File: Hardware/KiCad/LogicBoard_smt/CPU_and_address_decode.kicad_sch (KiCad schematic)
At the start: 20 parts, among them IC12 7408N, IC16 7404N, IC32 7432N, IC4 7404N, IC53 7404N, IC7 7408N, U1 W65C02SP, U2 VIA

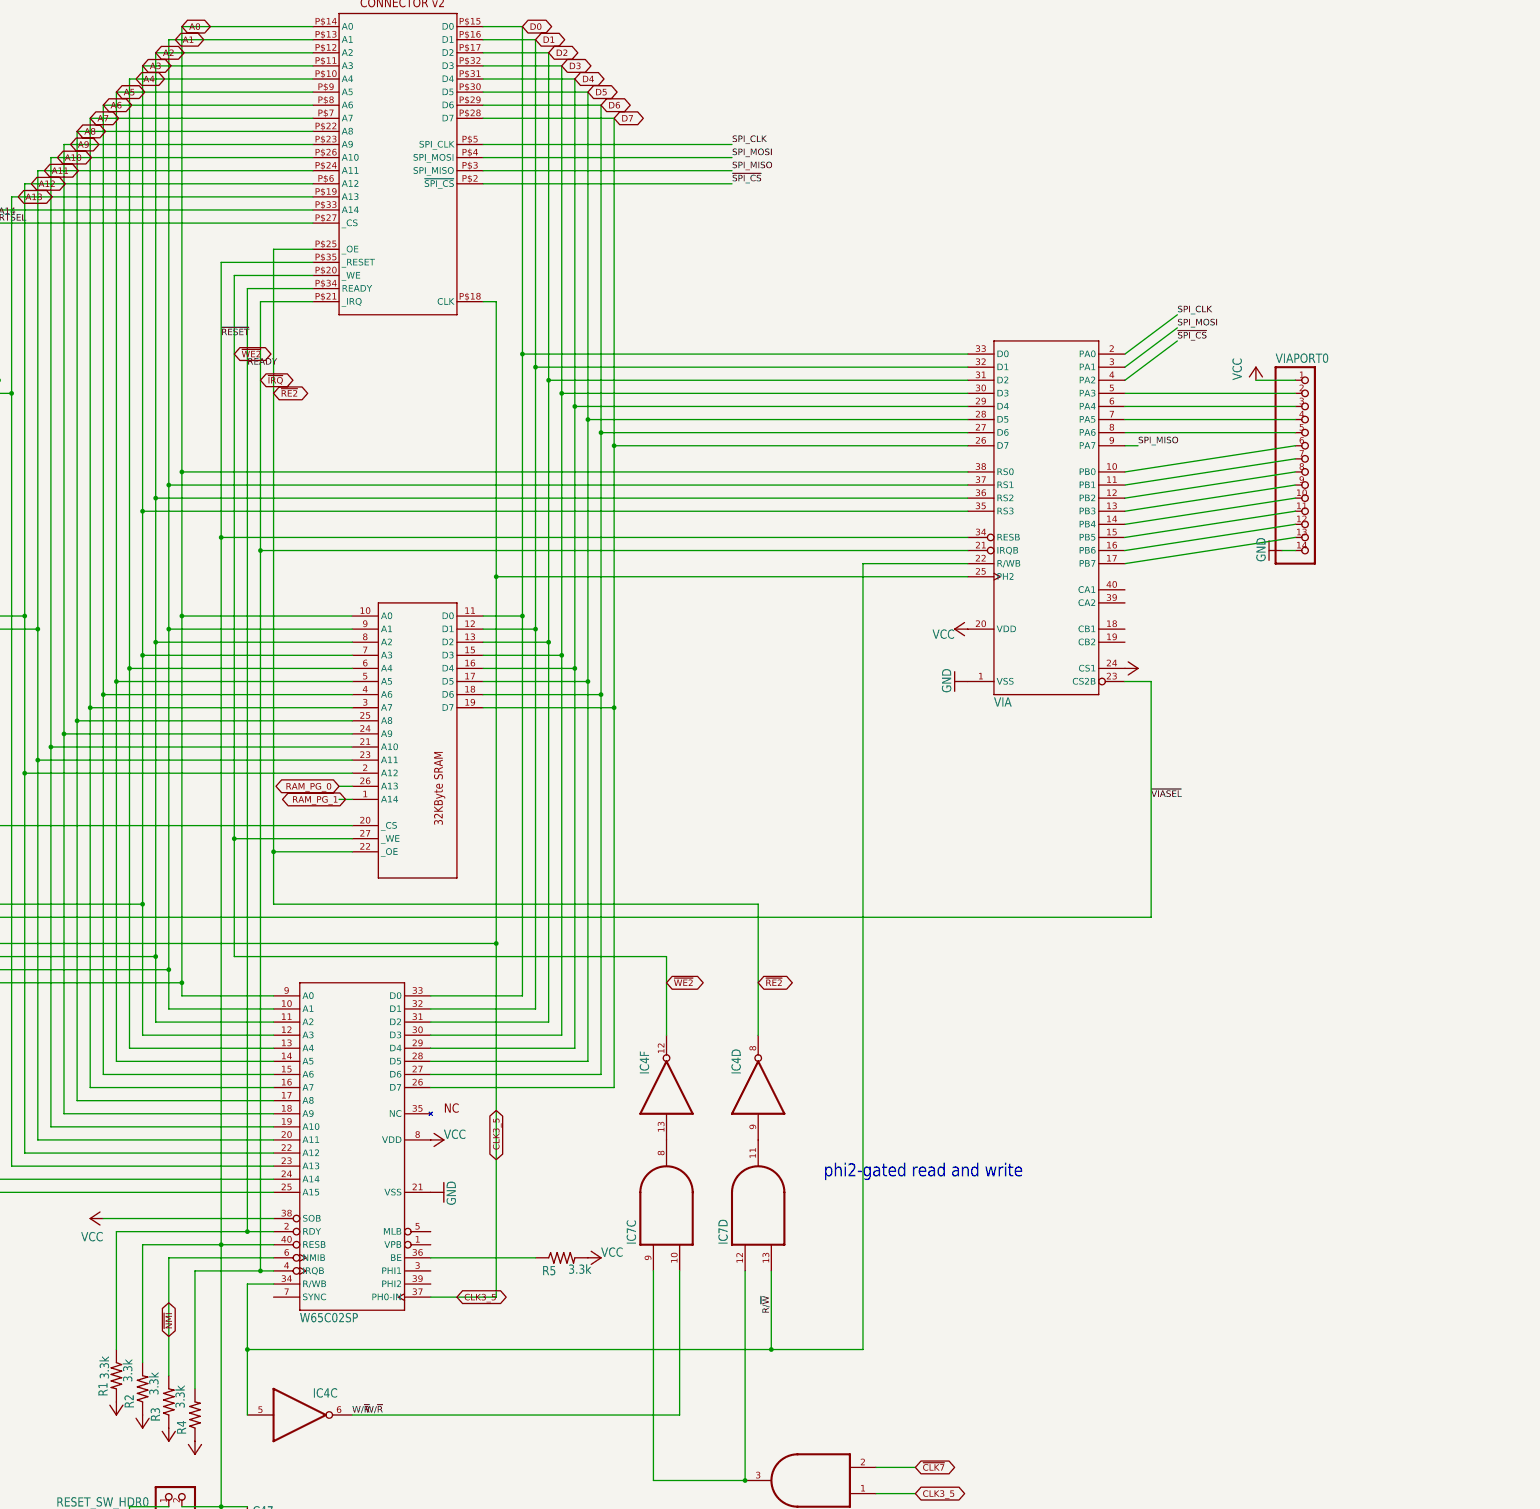
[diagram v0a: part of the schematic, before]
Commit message: updates to kicad smt versions
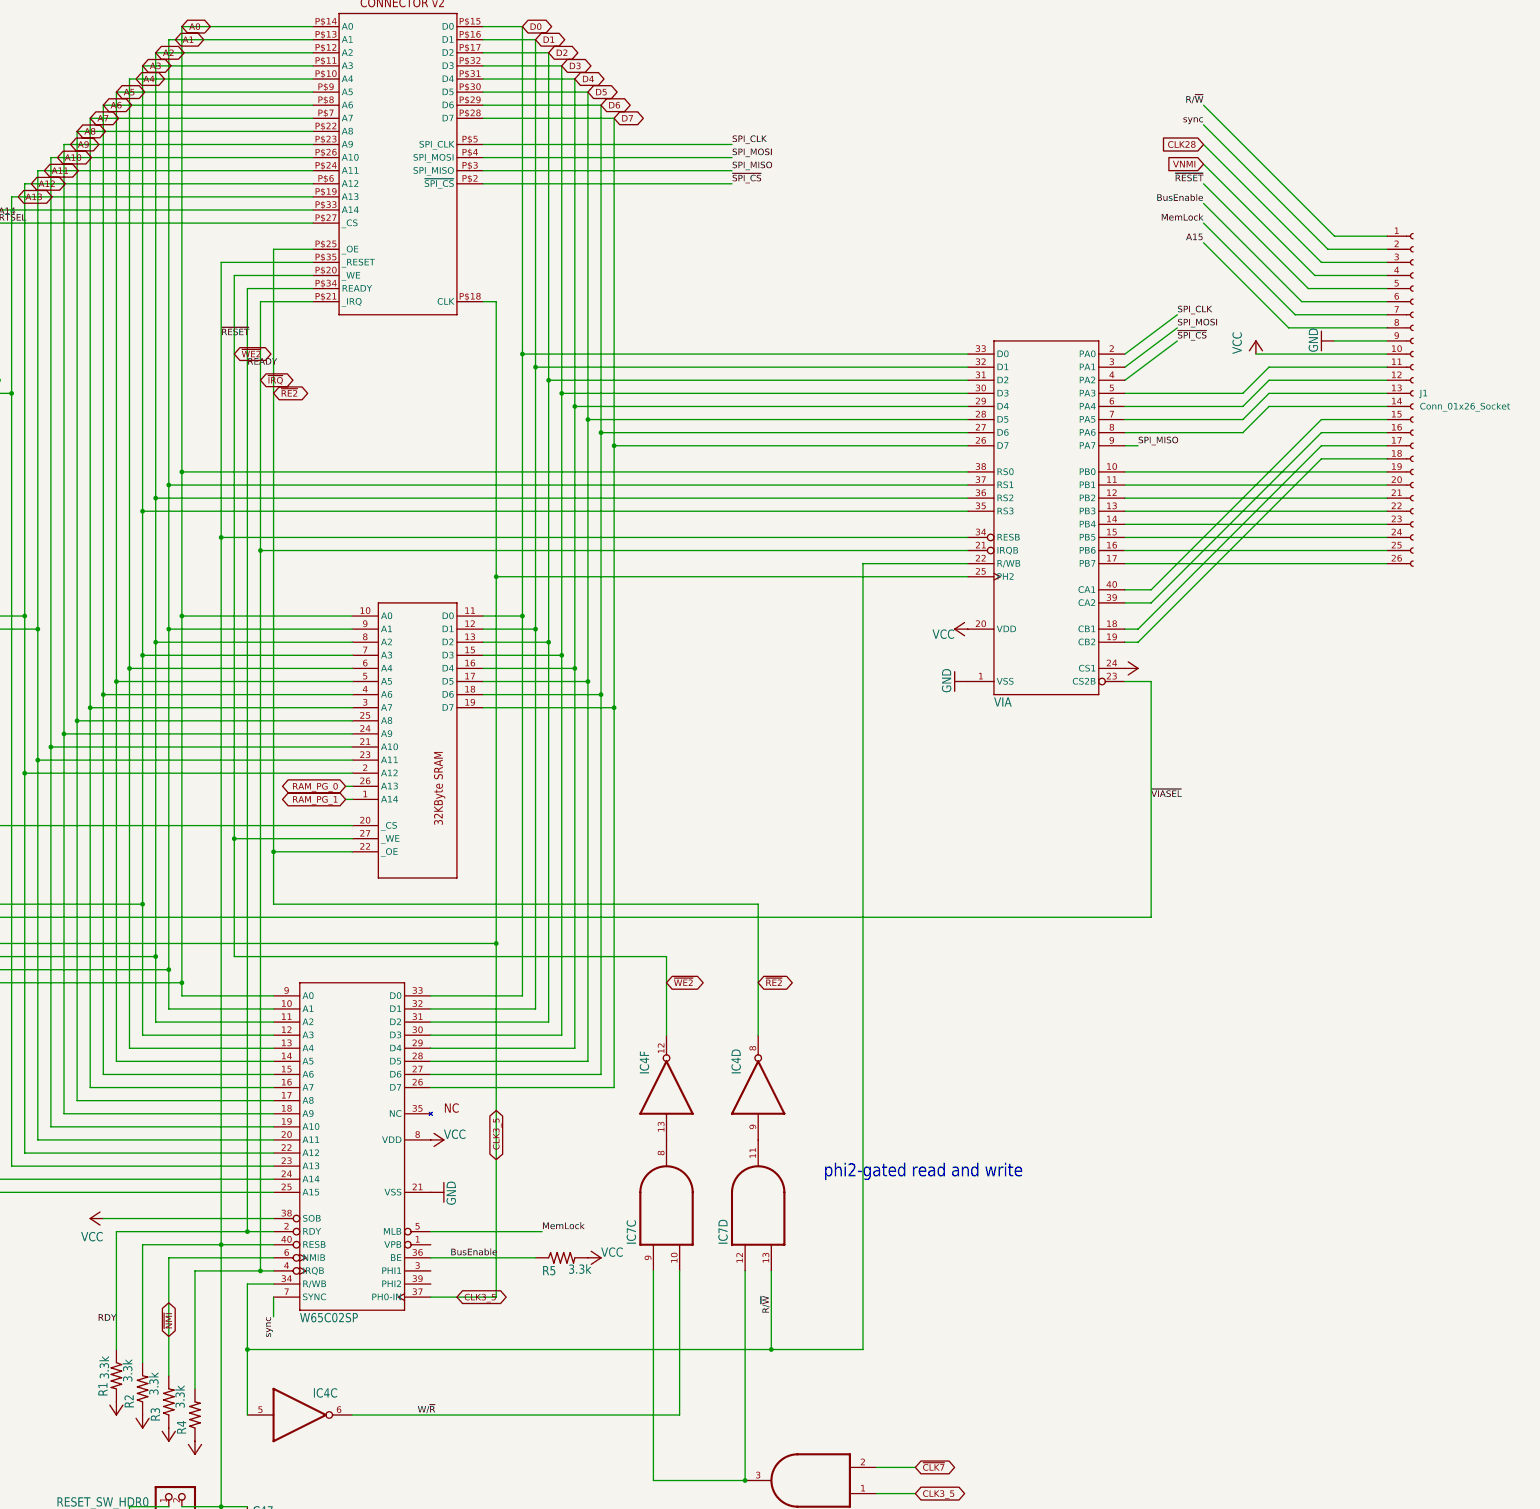
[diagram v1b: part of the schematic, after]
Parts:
- removed VIAPORT0: PINHD-1X14, Connector_PinSocket_2.54mm:PinSocket_1x14_P2.54mm_Horizontal, symbol cpu-blitter-inputs-eagle-import:PINHD-1X14
- added J1: Conn_01x26_Socket, Connector_Dsub:DSUB-26-HD_Female_Horizontal_P2.29x1.98mm_EdgePinOffset8.35mm_Housed_MountingHolesOffset10.89mm, symbol Connector:Conn_01x26_Socket
- U$3: MPN 5645235-4 -> 5530843-3
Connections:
- net A15: now also J1.8 (Pin_8)
- net GND: now also J1.9 (Pin_9)
- net VCC: now also J1.10 (Pin_10)
- net ~{RESET}: now also J1.5 (Pin_5)
- net at U2.14 (PB4): now also J1.23 (Pin_23)
- net at U2.15 (PB5): now also J1.24 (Pin_24)
- net at U2.16 (PB6): now also J1.25 (Pin_25)
- net at U2.17 (PB7): now also J1.26 (Pin_26)
- net at U2.5 (PA3): now also J1.11 (Pin_11)
- net at U2.6 (PA4): now also J1.12 (Pin_12)
- net at U2.7 (PA5): now also J1.13 (Pin_13)
- net at U2.8 (PA6): now also J1.14 (Pin_14)
- net at U2.10 (PB0): now also J1.19 (Pin_19)
- net at U2.11 (PB1): now also J1.20 (Pin_20)
- net at U2.12 (PB2): now also J1.21 (Pin_21)
- net at U2.13 (PB3): now also J1.22 (Pin_22)
- net BusEnable: now reaches R5.1, U1.36 (BE)
- net BusEnable: now also J1.6 (Pin_6)
- net MemLock: now reaches U1.5 (MLB)
- net MemLock: now also J1.7 (Pin_7)
- net sync: now reaches U1.7 (SYNC)
- net sync: now also J1.2 (Pin_2)
- net at U2.18 (CB1): now also J1.17 (Pin_17)
- net at U2.19 (CB2): now also J1.18 (Pin_18)
- net at U2.39 (CA2): now also J1.16 (Pin_16)
- net at U2.40 (CA1): now also J1.15 (Pin_15)
- net READY renamed RDY
- new net CLK28: J1.3 (Pin_3)
- new net R/~{W}: J1.1 (Pin_1)
- new net VNMI: J1.4 (Pin_4)

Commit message: manual and models and misc hardware file updates
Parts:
- J1: footprint Connector_Dsub:DSUB-26-HD_Female_Horizontal_P2.29x1.98mm_EdgePinOffset8.35mm_Housed_MountingHolesOffset10.89mm -> connector:HDL26-SL-B
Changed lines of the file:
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@@
       (effects (font (size 1.27 1.27)) (justify left))
     )
-    (property "Footprint" "Connector_Dsub:DSUB-26-HD_Female_Horizontal_P2.29x1.98mm_EdgePinOffset8.35mm_Housed_MountingHolesOffset10.89mm" (at 408.94 96.52 0)
+    (property "Footprint" "connector:HDL26-SL-B" (at 408.94 96.52 0)
       (effects (font (size 1.27 1.27)) hide)
     )

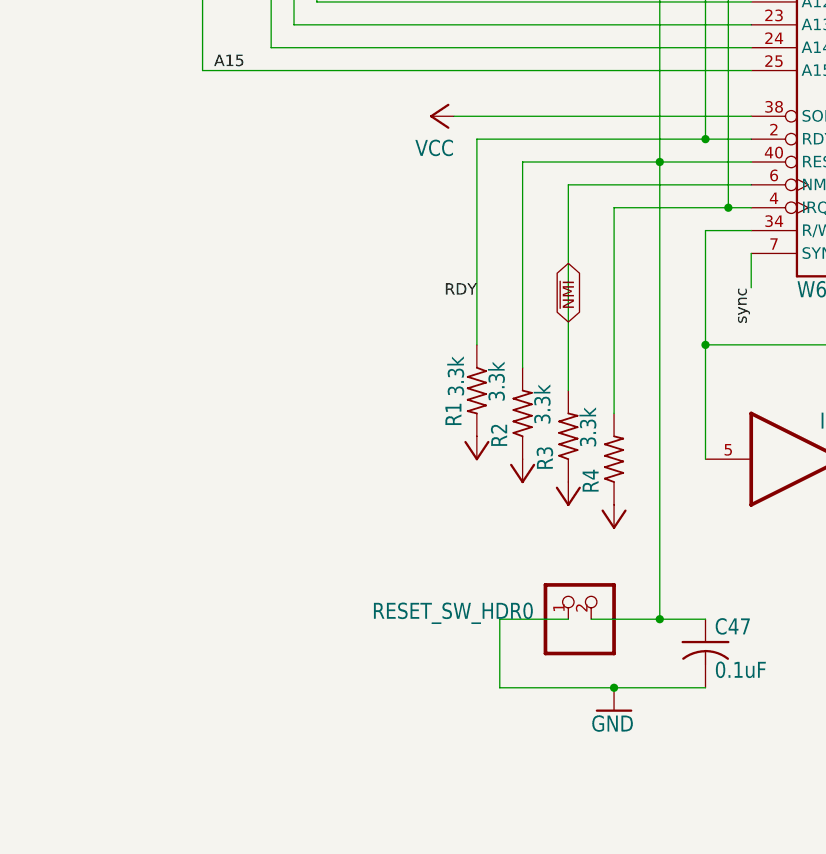
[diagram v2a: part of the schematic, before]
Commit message: add footprint for reset controller on logic board and remove READY on cartridges
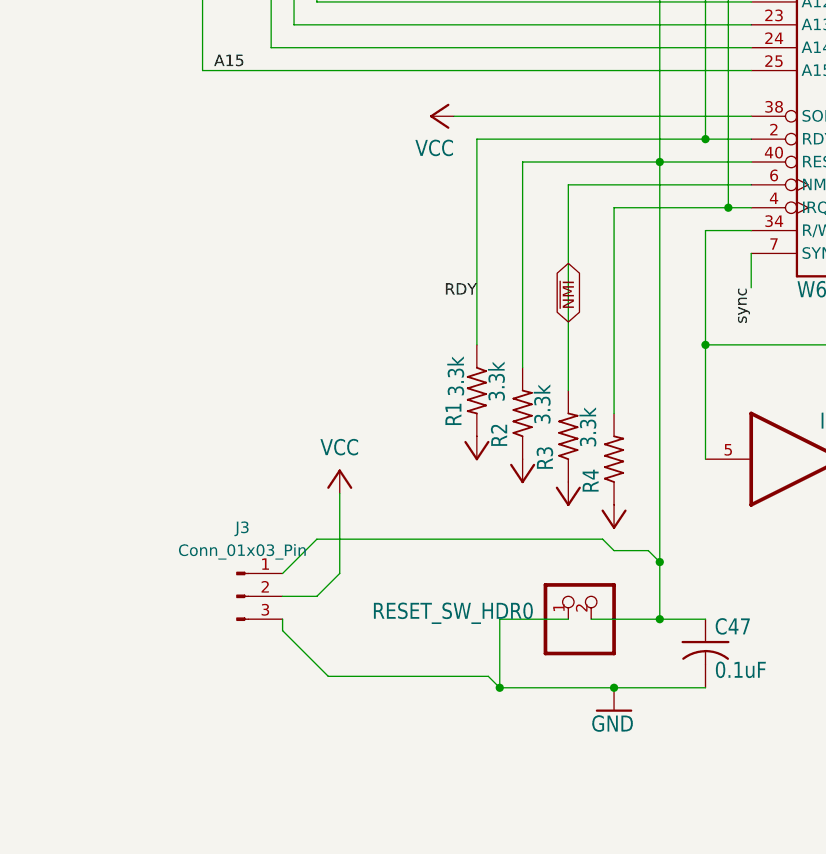
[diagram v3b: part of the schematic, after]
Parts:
- added J3: Conn_01x03_Pin, Connector_PinHeader_1.27mm:PinHeader_1x03_P1.27mm_Vertical, symbol Connector:Conn_01x03_Pin
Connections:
- net GND: now also J3.3 (Pin_3)
- net VCC: now also J3.2 (Pin_2)
- net ~{RESET}: now also J3.1 (Pin_1)
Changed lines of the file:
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@@
   (junction (at 165.1 144.78) (diameter 0) (color 0 0 0 0)
   )
+  (junction (at 160.02 320.04) (diameter 0) (color 0 0 0 0)
+  )
   (junction (at 147.32 406.4) (diameter 0) (color 0 0 0 0)
   )
@@
   (junction (at 200.66 429.26) (diameter 0) (color 0 0 0 0)
   )
+  (junction (at 177.8 306.07) (diameter 0) (color 0 0 0 0)
+  )
   (junction (at 243.84 147.32) (diameter 0) (color 0 0 0 0)
   )
@@
     (stroke (width 0.1524) (type solid))
   )
+  (wire (pts (xy 158.75 318.77) (xy 160.02 320.04))
+    (stroke (width 0) (type default))
+  )
   (wire (pts (xy 203.2 294.64) (xy 266.7 294.64))
     (stroke (width 0.1524) (type solid))
@@
     (stroke (width 0) (type default))
   )
+  (wire (pts (xy 135.89 313.69) (xy 140.97 318.77))
+    (stroke (width 0) (type default))
+  )
   (wire (pts (xy 113.03 407.67) (xy 113.03 406.4))
     (stroke (width 0) (type default))
@@
     (stroke (width 0.1524) (type solid))
   )
+  (wire (pts (xy 142.24 298.45) (xy 142.24 307.34))
+    (stroke (width 0) (type default))
+  )
   (wire (pts (xy 167.64 208.28) (xy 167.64 215.9))
     (stroke (width 0.1524) (type solid))
@@
     (stroke (width 0.1524) (type solid))
   )
+  (wire (pts (xy 139.7 303.53) (xy 171.45 303.53))
+    (stroke (width 0) (type default))
+  )
   (wire (pts (xy 381 99.06) (xy 403.86 99.06))
     (stroke (width 0) (type default))
@@
     (stroke (width 0) (type default))
   )
+  (wire (pts (xy 135.89 307.34) (xy 139.7 303.53))
+    (stroke (width 0) (type default))
+  )
   (wire (pts (xy 228.6 154.94) (xy 251.46 154.94))
     (stroke (width 0.1524) (type solid))
@@
     (stroke (width 0) (type default))
   )
-  (wire (pts (xy 177.8 261.62) (xy 177.8 312.42))
+  (wire (pts (xy 177.8 261.62) (xy 177.8 306.07))
     (stroke (width 0.1524) (type solid))
   )
@@
     (stroke (width 0.1524) (type solid))
   )
+  (wire (pts (xy 176.53 304.8) (xy 177.8 306.07))
+    (stroke (width 0) (type default))
+  )
   (wire (pts (xy 353.06 121.92) (xy 403.86 121.92))
     (stroke (width 0) (type default))
@@
     (stroke (width 0.1524) (type solid))
   )
+  (wire (pts (xy 172.72 304.8) (xy 176.53 304.8))
+    (stroke (width 0) (type default))
+  )
   (wire (pts (xy 322.58 111.76) (xy 170.18 111.76))
     (stroke (width 0.1524) (type solid))
@@
     (stroke (width 0.1524) (type solid))
   )
+  (wire (pts (xy 135.89 309.88) (xy 139.7 309.88))
+    (stroke (width 0) (type default))
+  )
   (wire (pts (xy 154.94 256.54) (xy 187.96 256.54))
     (stroke (width 0.1524) (type solid))
@@
     (stroke (width 0.1524) (type solid))
   )
+  (wire (pts (xy 139.7 309.88) (xy 142.24 307.34))
+    (stroke (width 0) (type default))
+  )
   (wire (pts (xy 170.18 213.36) (xy 187.96 213.36))
     (stroke (width 0.1524) (type solid))
@@
     (stroke (width 0.1524) (type solid))
   )
+  (wire (pts (xy 135.89 312.42) (xy 135.89 313.69))
+    (stroke (width 0) (type default))
+  )
   (wire (pts (xy 254 106.68) (xy 254 157.48))
     (stroke (width 0.1524) (type solid))
@@
     (stroke (width 0.1524) (type solid))
   )
+  (wire (pts (xy 177.8 306.07) (xy 177.8 312.42))
+    (stroke (width 0.1524) (type solid))
+  )
   (wire (pts (xy 246.38 99.06) (xy 246.38 149.86))
     (stroke (width 0.1524) (type solid))
@@
     (stroke (width 0) (type default))
   )
+  (wire (pts (xy 171.45 303.53) (xy 172.72 304.8))
+    (stroke (width 0) (type default))
+  )
   (wire (pts (xy 355.6 142.24) (xy 391.16 106.68))
     (stroke (width 0) (type default))
@@
   (wire (pts (xy 50.8 195.58) (xy 50.8 335.28))
     (stroke (width 0.1524) (type solid))
+  )
+  (wire (pts (xy 140.97 318.77) (xy 158.75 318.77))
+    (stroke (width 0) (type default))
   )
   (wire (pts (xy 182.88 259.08) (xy 187.96 259.08))
@@
         (path "/28034957-81b4-48a5-b869-6f4cb8f0c2fa/f0ce6048-bb8c-44d1-87fc-da575349d621"
           (reference "#P+033") (unit 1)
+        )
+      )
+    )
+  )
+  (symbol (lib_id "Connector:Conn_01x03_Pin") (at 130.81 309.88 0) (unit 1)
+    (in_bom yes) (on_board yes) (dnp no) (fields_autoplaced)
+    (property "Reference" "J3" (at 131.445 302.26 0)
+      (effects (font (size 1.27 1.27)))
+    )
+    (property "Value" "Conn_01x03_Pin" (at 131.445 304.8 0)
+      (effects (font (size 1.27 1.27)))
+    )
+    (property "Footprint" "Connector_PinHeader_1.27mm:PinHeader_1x03_P1.27mm_Vertical" (at 130.81 309.88 0)
+      (effects (font (size 1.27 1.27)) hide)
+    )
+    (property "Datasheet" "~" (at 130.81 309.88 0)
+      (effects (font (size 1.27 1.27)) hide)
+    )
+    (pin "1")
+    (pin "2")
+    (pin "3")
+    (instances
+      (project "LogicBoard_smt"
+        (path "/28034957-81b4-48a5-b869-6f4cb8f0c2fa/f0ce6048-bb8c-44d1-87fc-da575349d621"
+          (reference "J3") (unit 1)
         )
       )
@@
         )
       )
+    )
+  )
+  (symbol (lib_id "cpu-blitter-inputs-eagle-import:VCC") (at 142.24 295.91 0) (unit 1)
+    (in_bom yes) (on_board yes) (dnp no) (fields_autoplaced)
+    (property "Reference" "#P+037" (at 142.24 295.91 0)
+      (effects (font (size 1.27 1.27)) hide)
+    )
+    (property "Value" "VCC" (at 142.24 293.37 0)
+      (effects (font (size 1.778 1.5113)))
+    )
+    (property "Footprint" "" (at 142.24 295.91 0)
+      (effects (font (size 1.27 1.27)) hide)
+    )
+    (property "Datasheet" "" (at 142.24 295.91 0)
+      (effects (font (size 1.27 1.27)) hide)
+    )
+    (pin "1")
+    (instances
+      (project "LogicBoard_smt"
+        (path "/28034957-81b4-48a5-b869-6f4cb8f0c2fa/f0ce6048-bb8c-44d1-87fc-da575349d621"
+          (reference "#P+037") (unit 1)
+        )
+      )

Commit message: collect production documents for quoting
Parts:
- removed J3: Conn_01x03_Pin, Connector_PinHeader_1.27mm:PinHeader_1x03_P1.27mm_Vertical, symbol Connector:Conn_01x03_Pin
- added U8: MCP130-xxxxTT, Package_TO_SOT_SMD:SOT-23, symbol Power_Supervisor:MCP130-xxxxTT
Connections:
- net GND: now also U8.3 (VSS)
- net VCC: now also U8.2 (VDD)
- net ~{RESET}: now also U8.1 (~{RST})

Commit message: updates
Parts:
- RESET_SW_HDR0: footprint Connector_PinHeader_2.54mm:PinHeader_1x02_P2.54mm_Vertical_SMD_Pin1Right -> Connector_PinHeader_2.54mm:PinHeader_1x02_P2.54mm_Vertical; MPN TSM-102-01-L-SV-TR -> G800WC306018EU
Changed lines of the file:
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@@
 			)
 		)
-		(property "Footprint" "Connector_PinHeader_2.54mm:PinHeader_1x02_P2.54mm_Vertical_SMD_Pin1Right"
+		(property "Footprint" "Connector_PinHeader_2.54mm:PinHeader_1x02_P2.54mm_Vertical"
 			(at 170.18 309.88 0)
 			(effects
@@
 			)
 		)
-		(property "MPN" "TSM-102-01-L-SV-TR"
+		(property "MPN" "G800WC306018EU "
 			(at 170.18 309.88 0)
 			(effects
